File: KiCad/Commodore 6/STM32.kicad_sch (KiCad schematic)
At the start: 25 parts, among them J1 472192001, J2 FTSH-107-01-L-DV-K-A, SW4 SW_DPDT_x2, U1 STM32H562RIT6, U2 STM32H7A3RIT6, U3 NC7SZ19P6X

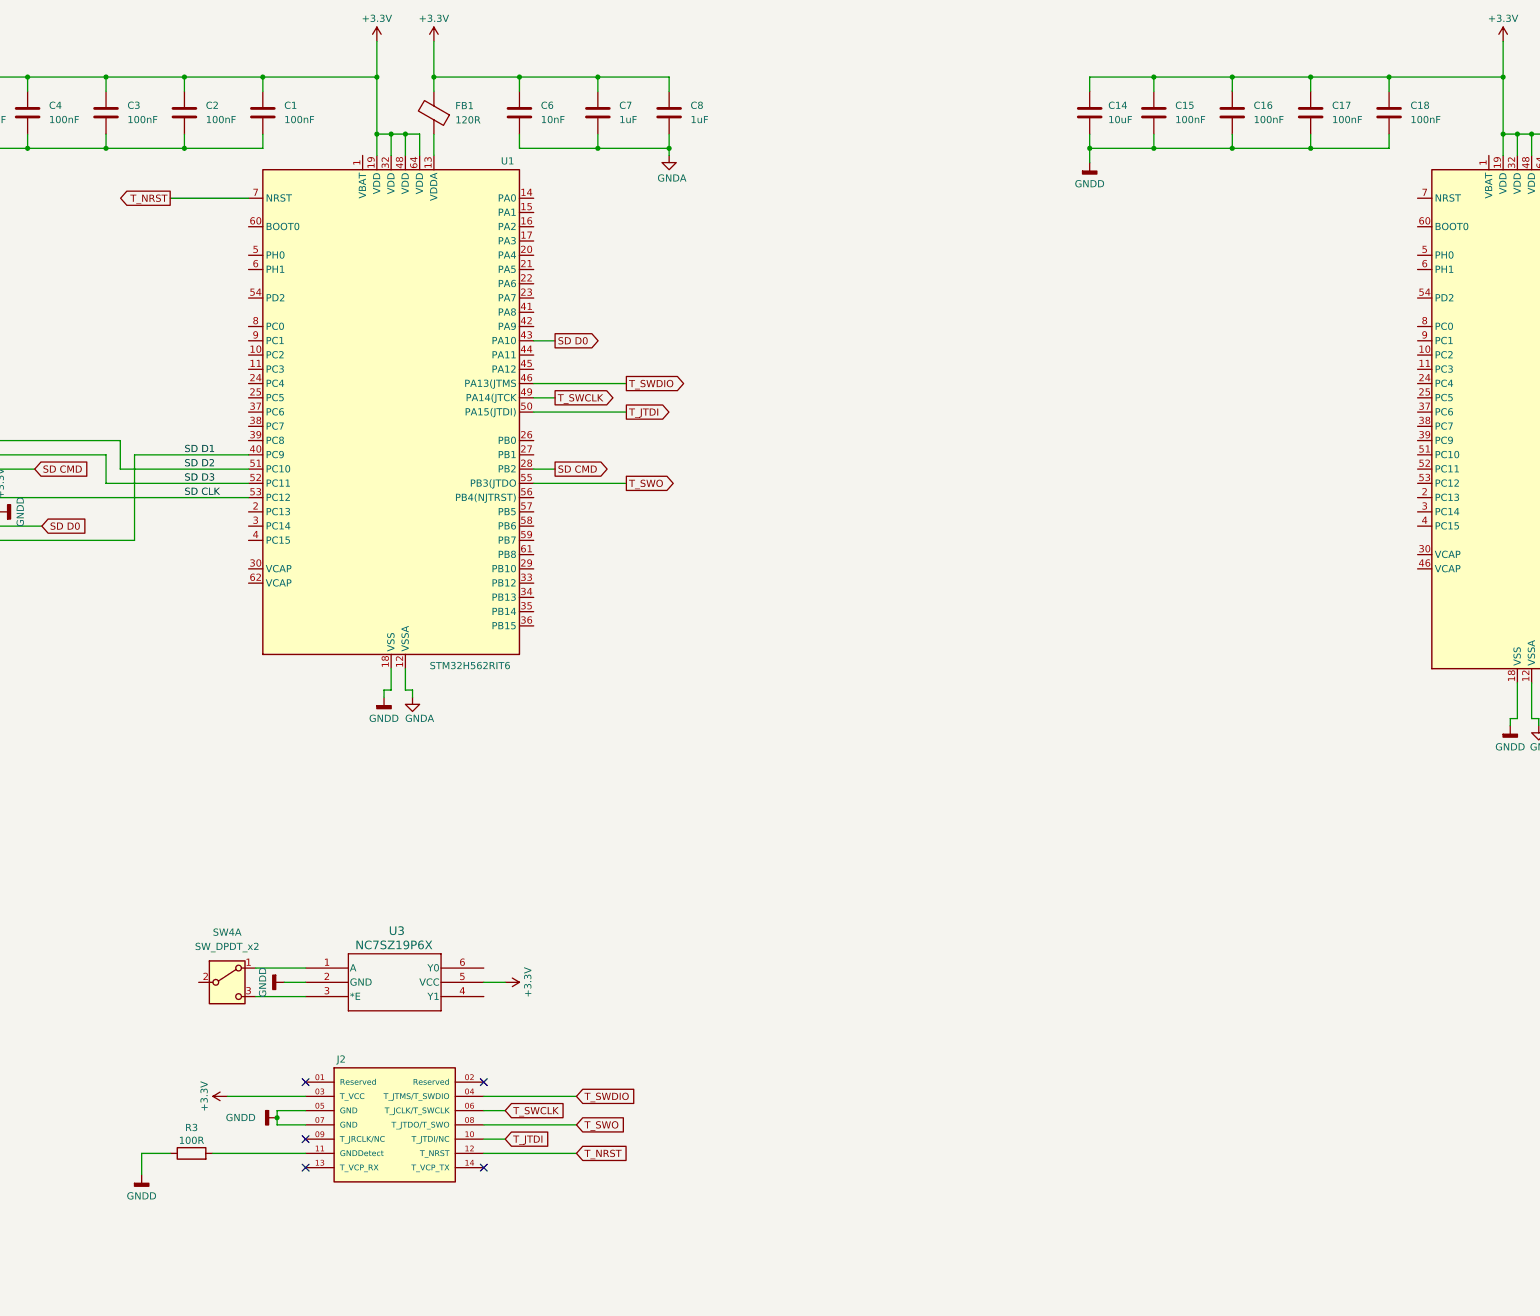
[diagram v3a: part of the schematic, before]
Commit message: Added DeMultiplexer
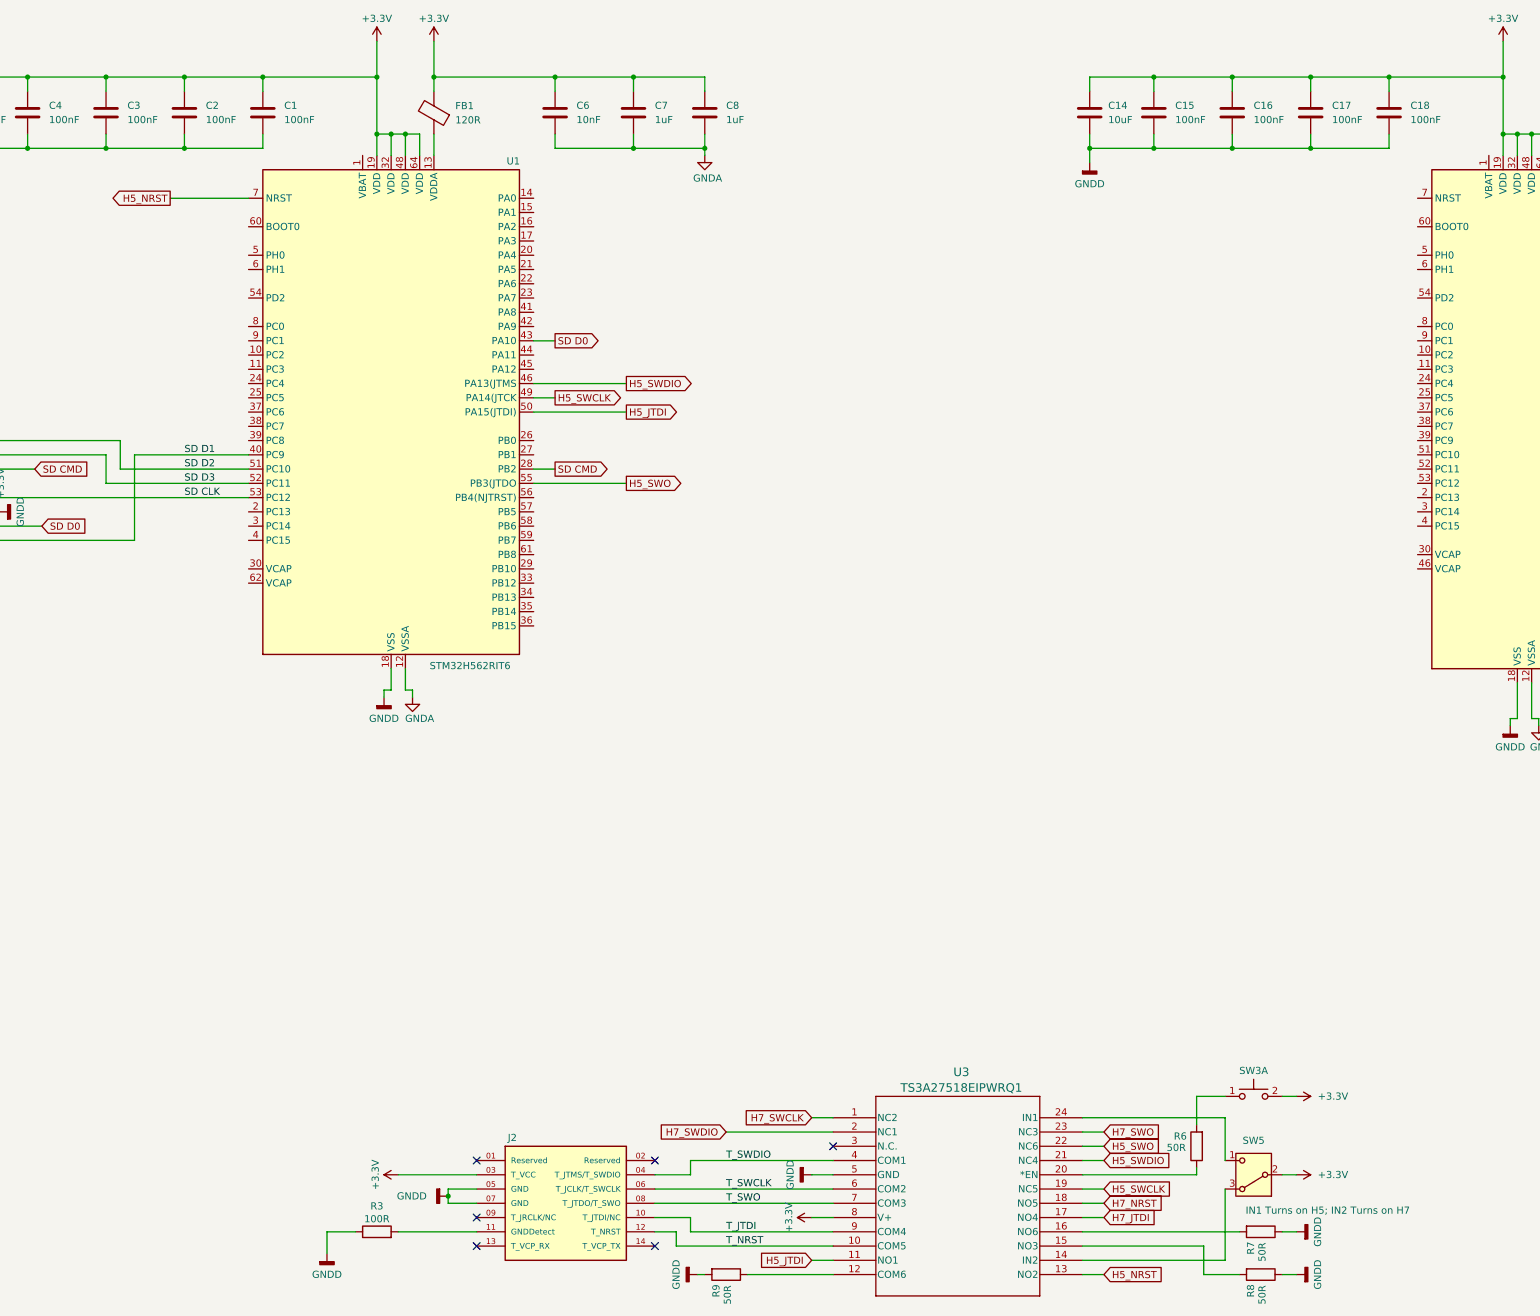
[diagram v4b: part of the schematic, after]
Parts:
- removed SW4: SW_DPDT_x2, symbol Switch:SW_DPDT_x2
- removed U3: NC7SZ19P6X, SOT363-6_FAS, symbol NC7SZ19P6X Demultiplexer:NC7SZ19P6X
- added R6, R7, R8, R9: 50R, symbol Device:R
- added SW3: SW_Push_Dual_x2, symbol Switch:SW_Push_Dual_x2
- added SW5: SW_Nidec_CAS-120A1, Button_Switch_SMD:Nidec_Copal_CAS-120A, symbol Switch:SW_Nidec_CAS-120A1
- added U3: TS3A27518EIPWRQ1, PW24, symbol TS3A27518EIPWRQ1 Demultiplexer:TS3A27518EIPWRQ1
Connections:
- net +3.3V: now also SW3.2 (D), SW5.2 (B), U3.8 (V+)
- net GNDD: now also R7.1, R8.1, R9.2, U3.5 (GND)
- net T_JTDI: now also U3.9 (COM4); no longer U1.50 (PA15(JTDI))
- net T_NRST: now also U3.10 (COM5); no longer U1.7 (NRST)
- net T_SWCLK: now also U3.6 (COM2); no longer U1.49 (PA14(JTCK)
- net T_SWDIO: now also U3.4 (COM1); no longer U1.46 (PA13(JTMS)
- net T_SWO: now also U3.7 (COM3); no longer U1.55 (PB3(JTDO)
- new net: R6.2, SW3.1 (C)
- new net: R7.2, U3.16 (NO6)
- new net: R6.1, U3.20 (*EN)
- new net: R9.1, U3.12 (COM6)
- new net: R8.2, U3.15 (NO3)
- new net: SW5.3 (A), U3.14 (IN2)
- new net: SW5.1 (C), U3.24 (IN1)
- new net H5_JTDI: U1.50 (PA15(JTDI)), U3.11 (NO1)
- new net H5_NRST: U1.7 (NRST), U3.13 (NO2)
- new net H5_SWCLK: U1.49 (PA14(JTCK), U3.19 (NC5)
- new net H5_SWDIO: U1.46 (PA13(JTMS), U3.21 (NC4)
- new net H5_SWO: U1.55 (PB3(JTDO), U3.22 (NC6)
- new net H7_JTDI: U3.17 (NO4)
- new net H7_NRST: U3.18 (NO5)
- new net H7_SWCLK: U3.1 (NC2)
- new net H7_SWDIO: U3.2 (NC1)
- new net H7_SWO: U3.23 (NC3)
- no-connect marks 5 -> 6
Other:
- moved on the sheet: C6, C7, C8, J2, R3

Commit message: Finished SWD Connector
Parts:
- added J5: FH12-24S-0.5SH_55_, FH12-24S-0.5SH_55_:HRS_FH12-24S-0.5SH_55_, symbol FH12_24S_0_5SH_55 Camera Connector:FH12-24S-0.5SH_55_
- added R10, R11: 50R, symbol Device:R
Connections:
- net H7_JTDI: now also U2.50 (PA15)
- net H7_NRST: now also U2.7 (NRST)
- net H7_SWCLK: now also U2.49 (PA14)
- net H7_SWDIO: now also U2.45 (PA13)
- net H7_SWO: now also U2.55 (PB3)
- net at SW5.3 (A): now also R11.1; no longer U3.14 (IN2)
- net at SW5.1 (C): now also R10.1; no longer U3.24 (IN1)
- new net: R11.2, U3.14 (IN2)
- new net: R10.2, U3.24 (IN1)
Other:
- moved on the sheet: J2, R3, R6, R7, R8, R9, SW3A, SW5, U3

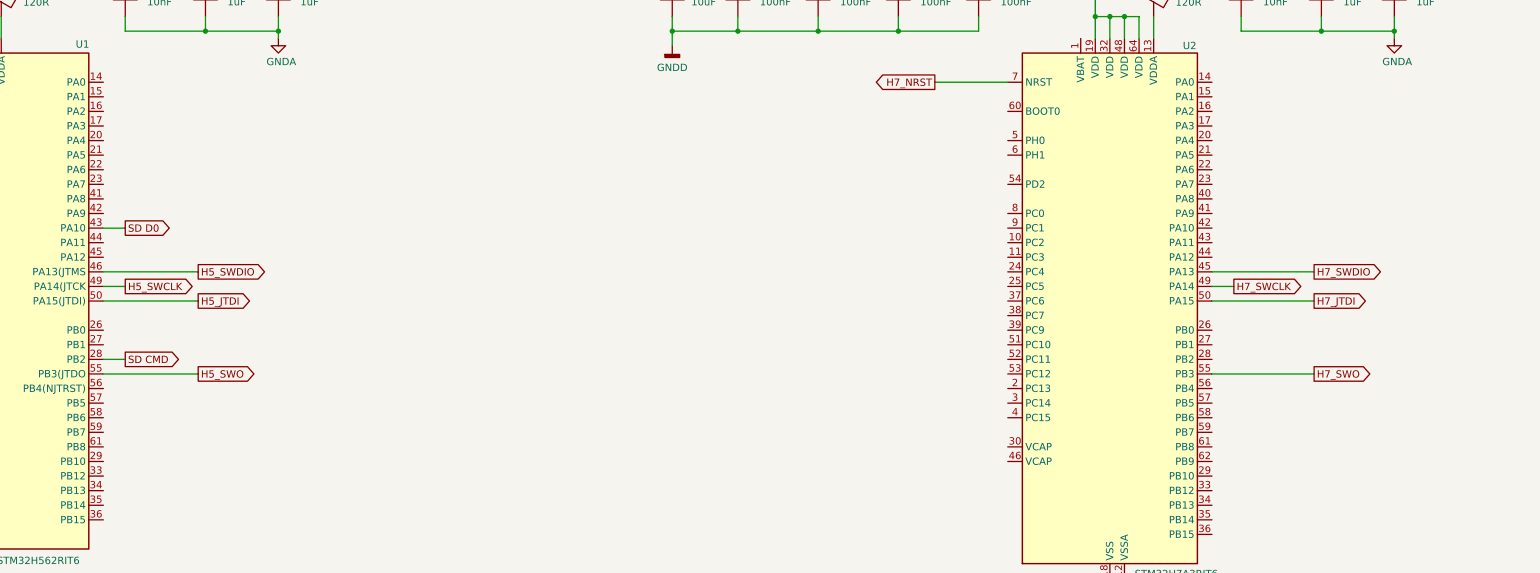
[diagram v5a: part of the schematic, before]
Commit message: label making and imported protection footprint
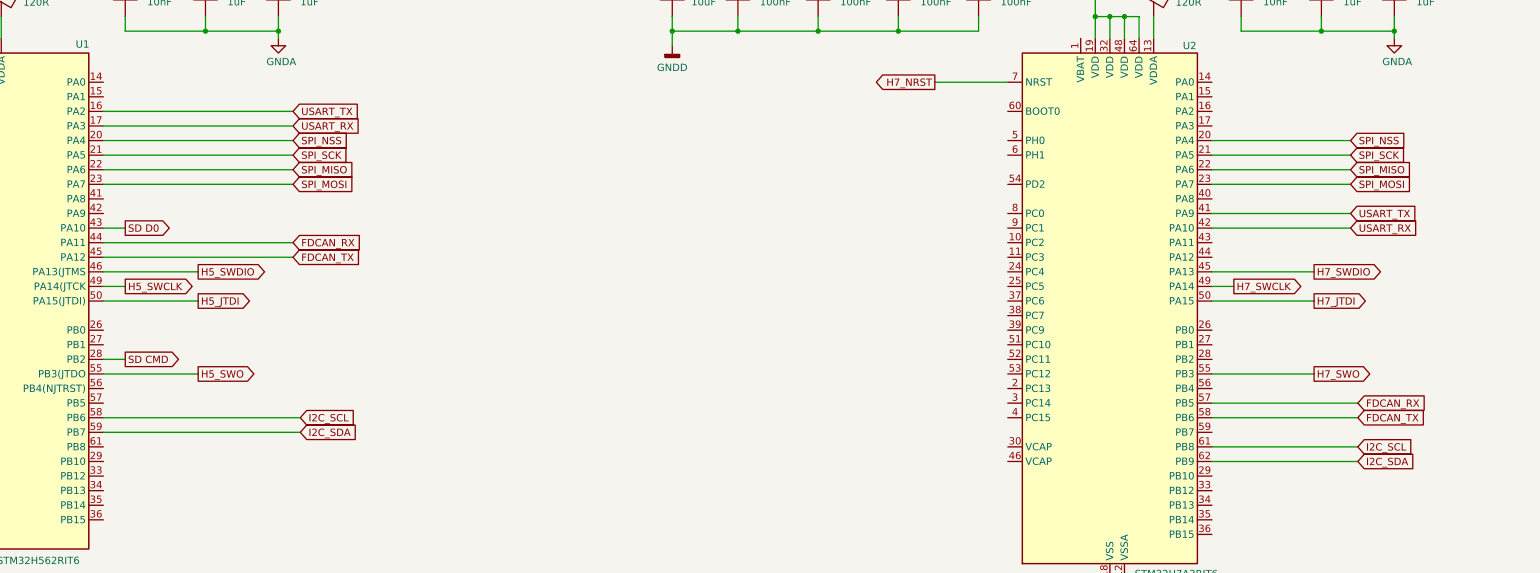
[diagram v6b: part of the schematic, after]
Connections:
- net SPI_NSS: now reaches U2.20 (PA4)
- net SPI_NSS: now also U1.20 (PA4)
- net SPI_SCK: now reaches U2.21 (PA5)
- net SPI_SCK: now also U1.21 (PA5)
- net SPI_MISO: now reaches U2.22 (PA6)
- net SPI_MISO: now also U1.22 (PA6)
- net SPI_MOSI: now reaches U2.23 (PA7)
- net SPI_MOSI: now also U1.23 (PA7)
- net USART_TX: now reaches U2.41 (PA9)
- net USART_TX: now also U1.16 (PA2)
- net USART_RX: now reaches U2.42 (PA10)
- net USART_RX: now also U1.17 (PA3)
- net FDCAN_RX: now reaches U2.57 (PB5)
- net FDCAN_RX: now also U1.44 (PA11)
- net FDCAN_TX: now reaches U2.58 (PB6)
- net FDCAN_TX: now also U1.45 (PA12)
- net I2C_SCL: now reaches U2.61 (PB8)
- net I2C_SCL: now also U1.58 (PB6)
- net I2C_SDA: now reaches U2.62 (PB9)
- net I2C_SDA: now also U1.59 (PB7)

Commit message: I'm Hungry (Added Camera Connectors)
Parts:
- added C24, C25: 100nF, symbol Device:C
- added J7: FH12-22S-0.5SH55, CONN_FH12-22S-0.5SH55_HIR, symbol FH12_22S_0_5SH_55 C2I Camera Connector:FH12-22S-0.5SH55
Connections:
- net GNDA: now also J5.2 (AGND)
- net GNDD: now also J5.15 (GND)
- net H5_NRST: now also C24.1; no longer U1.7 (NRST)
- net H7_NRST: now also C25.1; no longer U2.7 (NRST)
- net DCMI_D2: now reaches U2.34 (PB13)
- net DCMI_D2: now also J5.19 (Y2)
- net DCMI_D3: now reaches U2.39 (PC9)
- net DCMI_D3: now also J5.21 (Y3)
- net DCMI_D8: now reaches U2.51 (PC10)
- net DCMI_D8: now also J5.14 (Y8)
- net DCMI_D4: now reaches U2.52 (PC11)
- net DCMI_D4: now also J5.22 (Y4)
- net DCMI_D9: now reaches U2.53 (PC12)
- net DCMI_D9: now also J5.12 (Y9)
- net DCMI_VSYNC: now reaches U2.59 (PB7)
- net DCMI_VSYNC: now also J5.7 (VSYNC)
- net DCMI_D7: now reaches J5.16 (Y7)
- net DCMI_PIXCLK: now reaches J5.17 (PCLK)
- net DCMI_D6: now reaches J5.18 (Y6)
- net DCMI_D5: now reaches J5.20 (Y5)
- net DCMI_SDA: now reaches J5.3 (SDA)
- net DCMI_SCL: now reaches J5.5 (SCL)
- net DCMI_HSYNC: now reaches J5.9 (HSYNC)
- new net: C25.2, U2.7 (NRST)
- new net: C24.2, U1.7 (NRST)
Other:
- moved on the sheet: J5
